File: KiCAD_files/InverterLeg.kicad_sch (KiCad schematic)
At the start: 61 parts, among them J803 Conn_01x01_Pin, J806 Conn_01x01_Pin, J811 Screw_Terminal_01x01, J814 Screw_Terminal_01x01, J817 Screw_Terminal_01x01, J825 Conn_02x02_Top_Bottom, J827 Conn_02x02_Top_Bottom, J831 Conn_02x02_Top_Bottom, Q801 IPT60R055CM8, Q802 IPT60R055CM8, T801 CMB1670V, T802 CMB1670V, U603 UCC21222DR, U704 VPS8701B, U707 VPS8701B, U811 TMP117xxDRV, U815 TMP117xxDRV

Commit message: First routing complete.
Signed-off-by: Jean Alinei <jean.alinei@owntech.org>
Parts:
- removed R710: 4.7k, Resistor_SMD:R_0603_1608Metric, symbol Device:R
- added C718, C719: 10uF, Capacitor_SMD:C_0805_2012Metric, symbol Device:C
- added R610, R611, R612, R613: 51R, Resistor_SMD:R_0402_1005Metric, symbol Device:R
- added U801, U802: LT1761-SD, Package_TO_SOT_SMD:TSOT-23-5, symbol Regulator_Linear:LT1761-SD
- U603: footprint Package_SO:SOIC-16W_7.5x10.3mm_P1.27mm -> Footprints:SOIC-16W_7.5x10.3mm_P1.27mm
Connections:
- net 12V_{HS}: now also C719.1, R610.2, U801.5 (VOUT); no longer C734.1, D709.1 (K), D710.1 (K)
- net 12V_{LS}: now also C718.1, R612.2, U802.5 (VOUT); no longer C717.1, C731.1, D703.1 (K), D704.1 (K), L706.1
- net GND_{LS}: now also C718.2, R613.1, U802.2 (GND)
- net K_{SWN}: now also C719.2, R611.1, U801.2 (GND)
- new net: C734.1, D709.1 (K), D710.1 (K), U801.1 (VIN), U801.3 (~{SHDN})
- new net: R610.1, R611.2, U801.4 (ADJ)
- new net: R612.1, R613.2, U802.4 (ADJ)
- new net 12V_{LSRAW}: C717.1, C731.1, D703.1 (K), D704.1 (K), L706.1, U802.1 (VIN), U802.3 (~{SHDN})

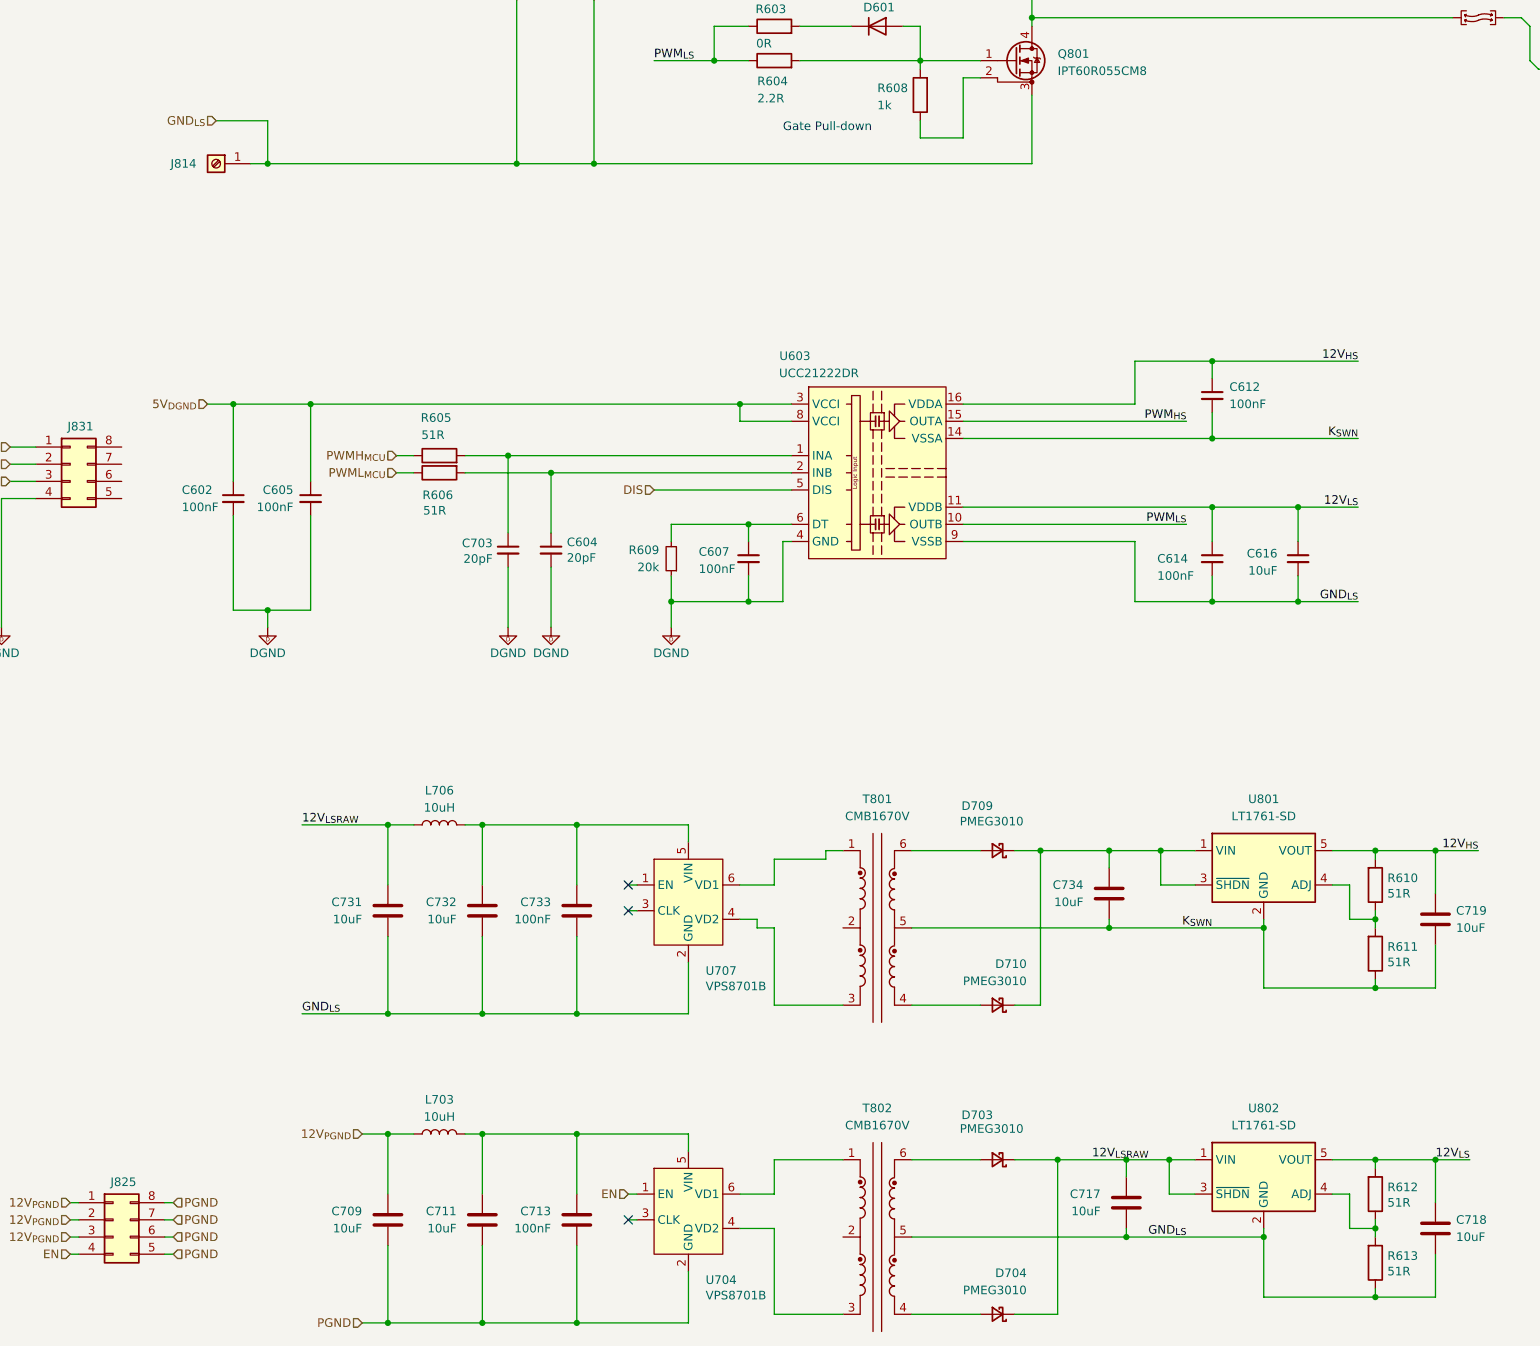
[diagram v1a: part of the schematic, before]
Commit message: Added gate coax. Added IPC2221 B1 rules. Changed diode footprints. Completed layout.
Signed-off-by: Jean Alinei <jean.alinei@owntech.org>
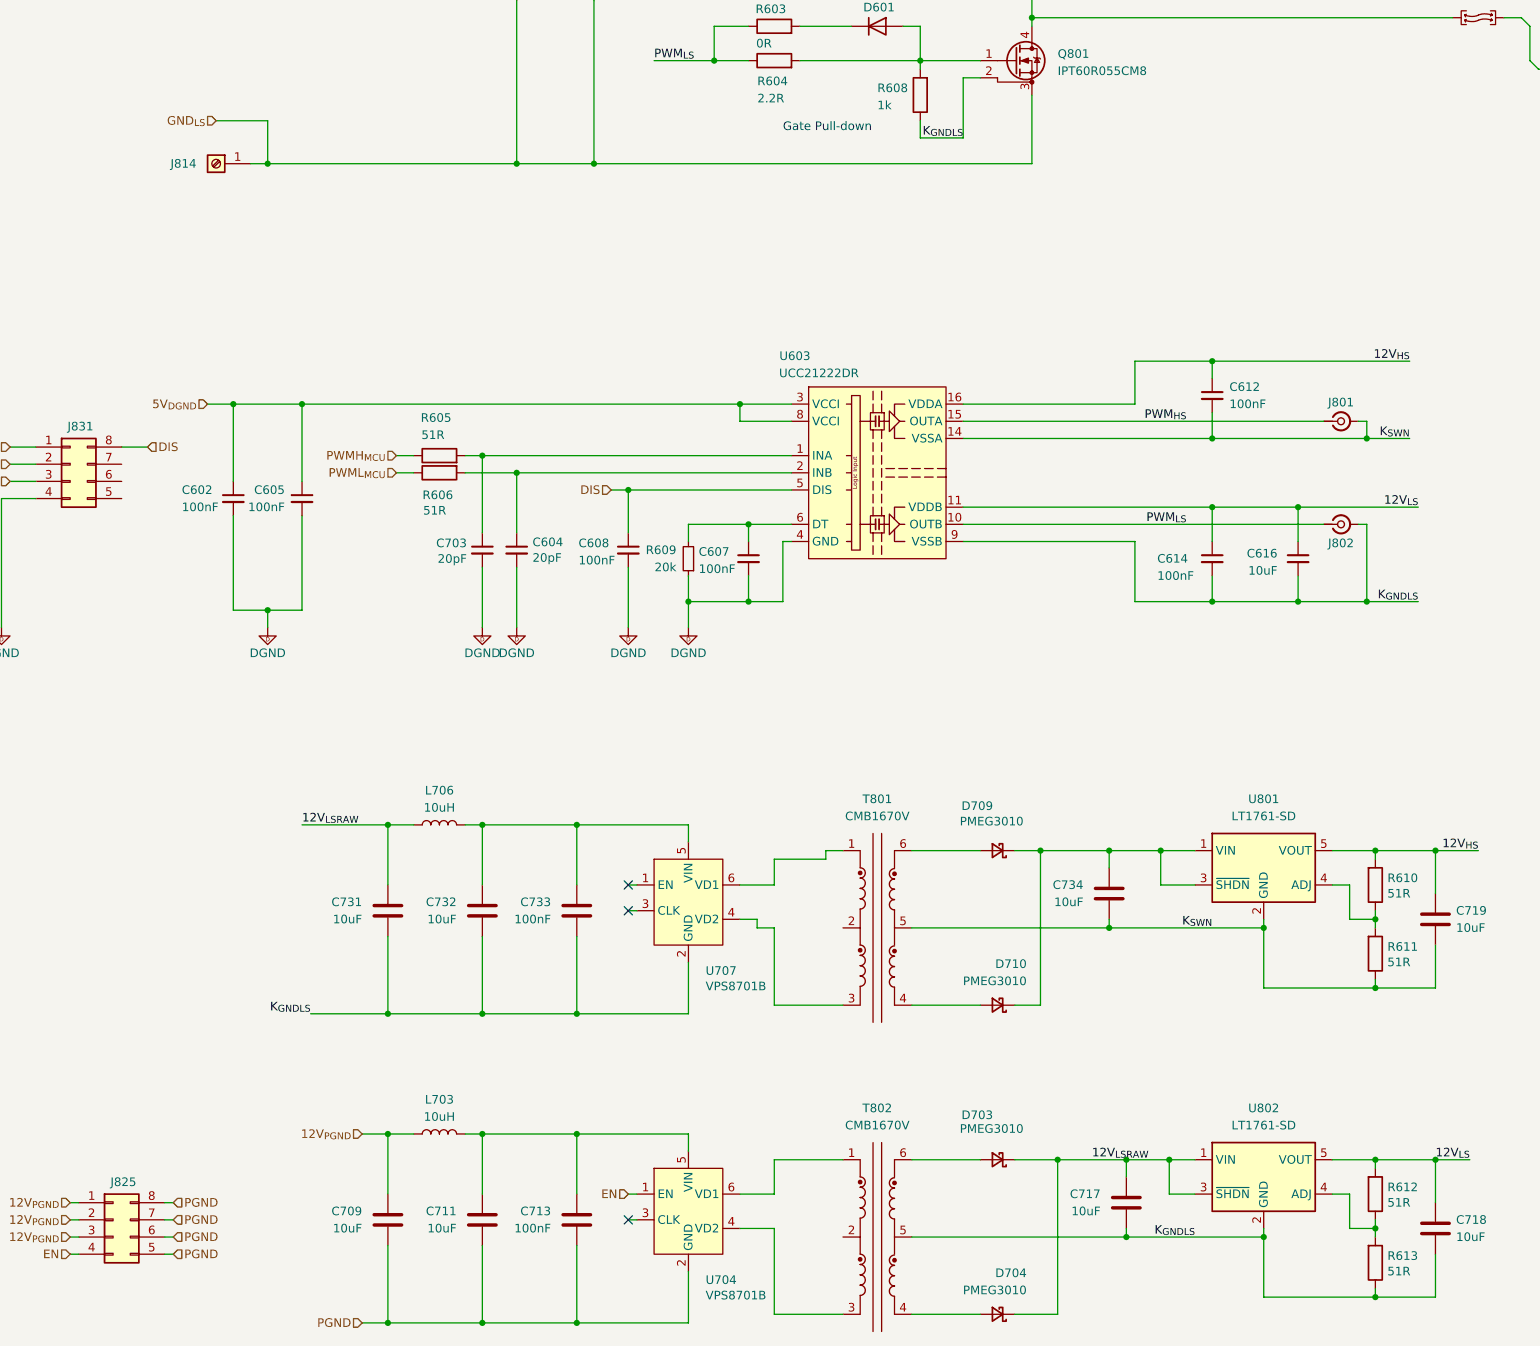
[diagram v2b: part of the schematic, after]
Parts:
- added C608: 100nF, Capacitor_SMD:C_0603_1608Metric, symbol Device:C_Small
- added J801, J802: Conn_Coaxial_Small, Footprints:IPEX-SMD_4P-L1.7-W1.7-LS2.0-L-4, symbol Symbols:Conn_Coaxial_Small
- D601: footprint Diode_SMD:D_SOD-323_HandSoldering -> Diode_SMD:D_SOD-882
- D602: value PMEG3010CEJ,115 -> (none); footprint Diode_SMD:D_SOD-323_HandSoldering -> Diode_SMD:D_SOD-882; manf# PMEG2010AEJ,115 -> (none)
- D703, D704, D709, D710: footprint Diode_SMD:D_SOD-323F -> Diode_SMD:D_SOD-882
- R607, R608: footprint Resistor_SMD:R_0603_1608Metric -> Resistor_SMD:R_0402_1005Metric
- TJ801, TJ804: footprint Resistor_SMD:R_1206_3216Metric -> Footprints:THJP_1206_3216Metric
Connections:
- net DGND: now also C608.2
- net DIS: now also J831.8 (Pin_8), C608.1
- net GND_{LS}: no longer C614.2, C616.2, C717.2, C718.2, C731.2, C732.2, C733.2, R613.1, T802.5, U603.9 (VSSB), U707.2 (GND), U802.2 (GND)
- net K_{SWN}: now also J801.2 (Ext), J801.3 (Ext), J801.4 (Ext)
- net PWM_{HS}: now also J801.1 (In)
- net PWM_{LS}: now also J802.1 (In)
- net K_{GNDLS}: now reaches Q801.2 (DS), R608.1
- net K_{GNDLS}: now also C614.2, C616.2, C717.2, C718.2, C731.2, C732.2, C733.2, R613.1, T802.5, U603.9 (VSSB), U707.2 (GND), U802.2 (GND), J802.2 (Ext), J802.3 (Ext), J802.4 (Ext)
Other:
- moved on the sheet: C604, C605, C703, R609

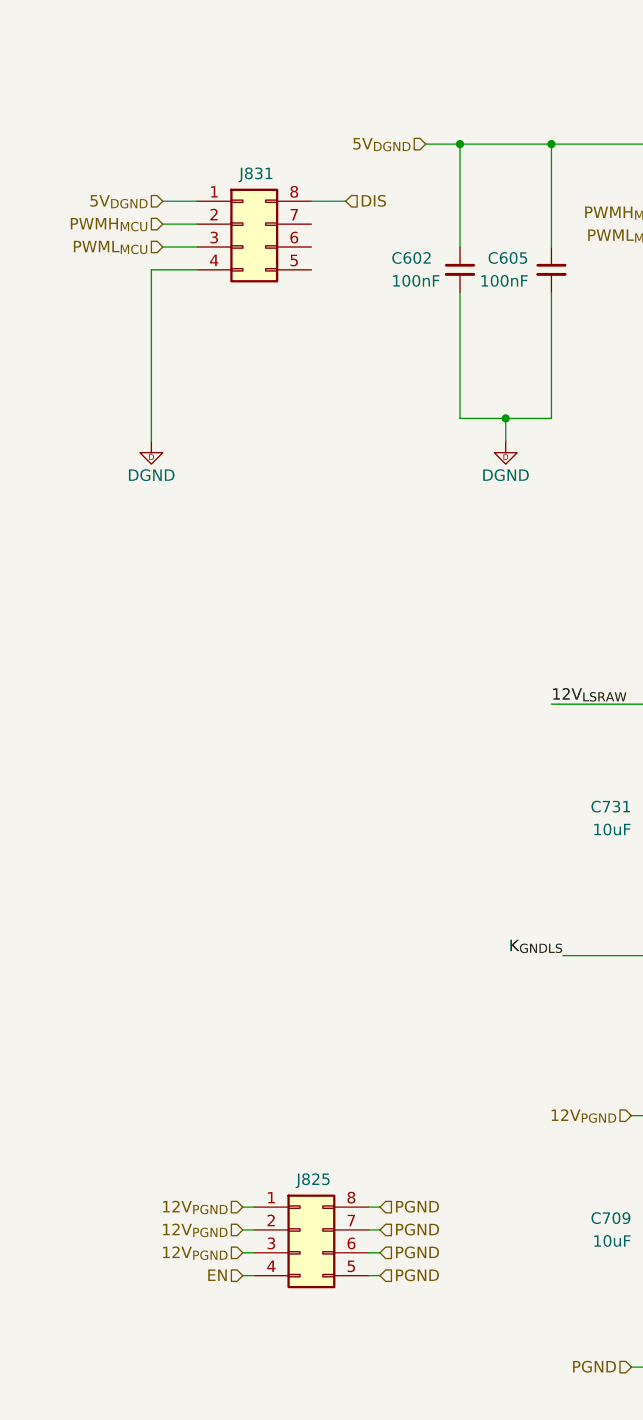
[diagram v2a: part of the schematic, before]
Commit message: Added SMTSO footprints to replace cube screw terminals. Added header for optional fan
Signed-off-by: Jean Alinei <jean.alinei@owntech.org>
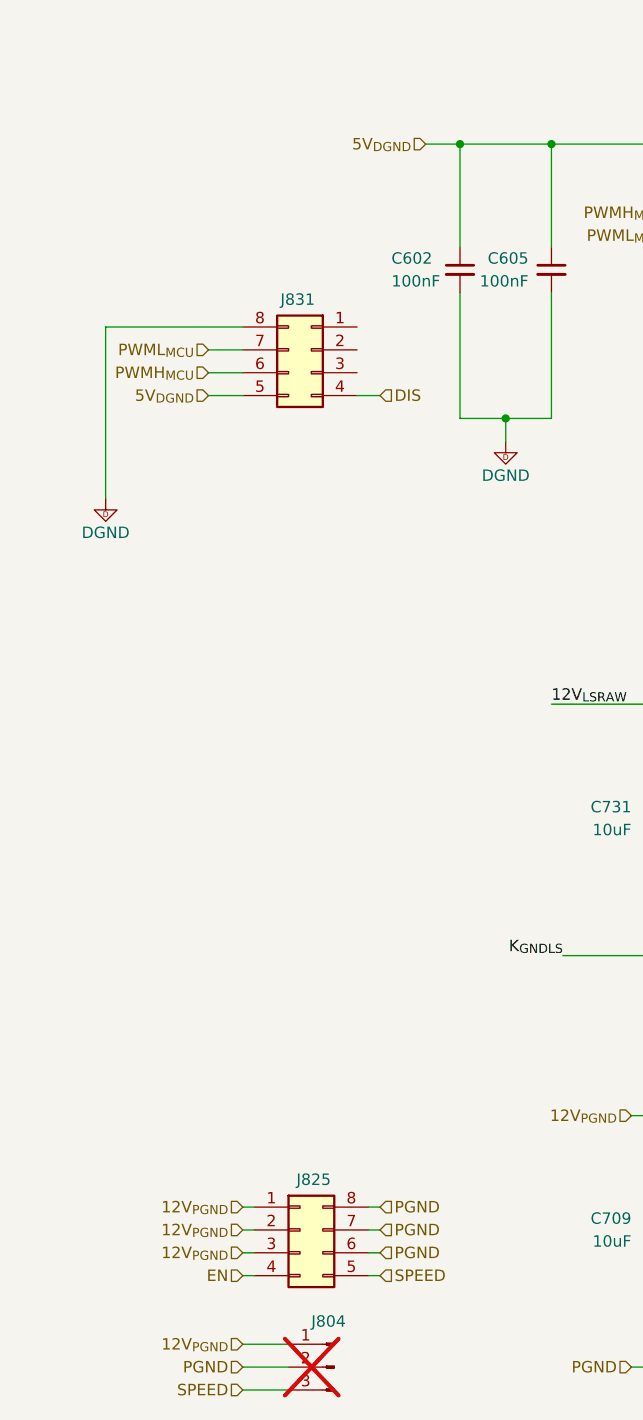
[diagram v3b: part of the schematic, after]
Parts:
- added J804: Conn_01x03_Socket, Connector_PinHeader_2.54mm:PinHeader_1x03_P2.54mm_Vertical, symbol Connector:Conn_01x03_Pin
- J801, J802: LCSC (none) -> C41432125
- J803, J806: LCSC (none) -> C54935091
- J811, J814, J817: footprint Footprints:SMD_L5.0-W5.0_CON1_5X5_SMD -> Footprints:SMD-1_BD5.5-D4.0_H5
- U801, U802: LCSC (none) -> C98119
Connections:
- net 12V_{PGND}: now also J804.1 (Pin_1)
- net 5V_{DGND}: now also J831.5 (Pin_5); no longer J831.1 (Pin_1)
- net DGND: now also J831.8 (Pin_8); no longer J831.4 (Pin_4)
- net DIS: now also J831.4 (Pin_4); no longer J831.8 (Pin_8)
- net PGND: now also J804.2 (Pin_2); no longer J825.5 (Pin_5)
- net PWMH_{MCU}: now also J831.6 (Pin_6); no longer J831.2 (Pin_2)
- net PWML_{MCU}: now also J831.7 (Pin_7); no longer J831.3 (Pin_3)
- new net SPEED: J804.3 (Pin_3), J825.5 (Pin_5)

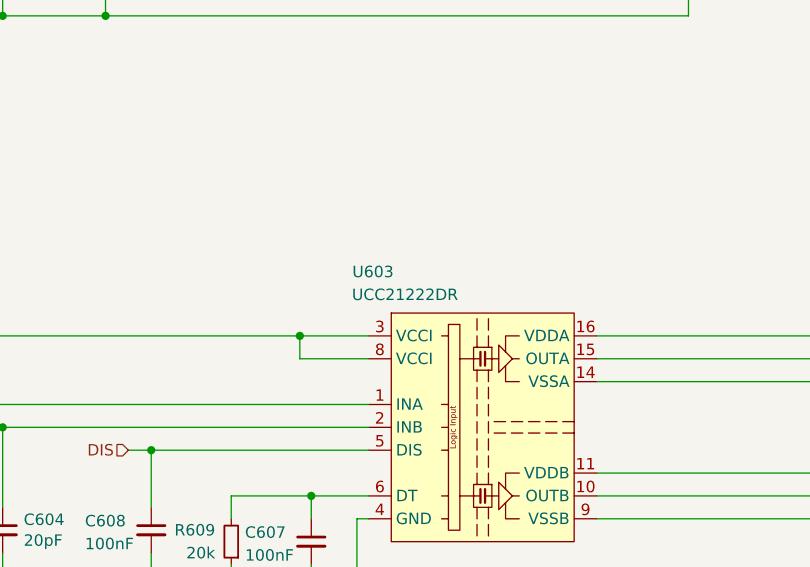
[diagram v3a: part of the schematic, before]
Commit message: Tidied up schematic - Final height for SMTSO 5mm
Signed-off-by: Jean Alinei <jean.alinei@owntech.org>
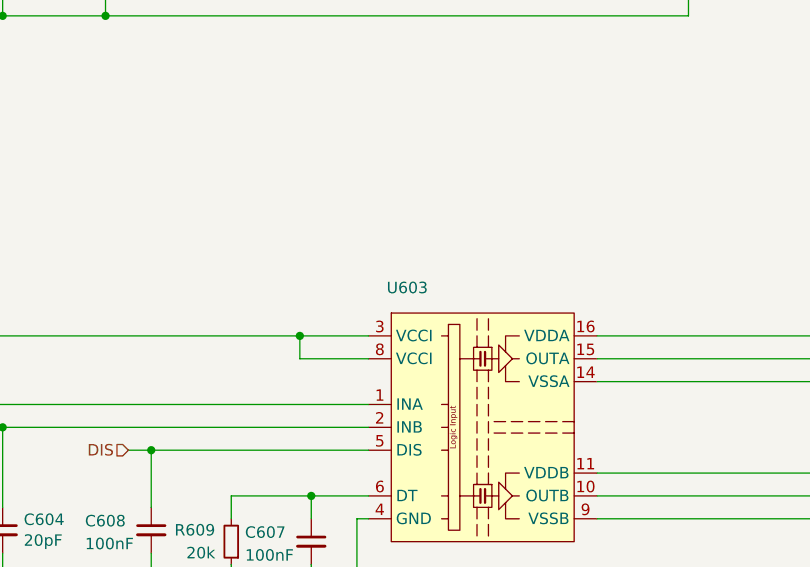
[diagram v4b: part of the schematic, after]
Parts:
- U603: value UCC21222DR -> (none); Reserved1 bccaf22d96de636e419712282ae246d314e74c1c3b4854d5 -> (none); manf# UCC21222DR -> (none)
- U704: LCSC (none) -> C5189123; Reserved1 54ac28721298fbc865f2e5f34cb150e57d7a5c0d0331fcf6 -> (none)
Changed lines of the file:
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@@
 		(dnp no)
 		(property "Reference" "U603"
-			(at 175.768 119.888 0)
-			(show_name no)
-			(do_not_autoplace no)
-			(effects
-				(font
-					(size 1.27 1.27)
-				)
-			)
-		)
-		(property "Value" "UCC21222DR"
+			(at 179.578 121.666 0)
+			(show_name no)
+			(do_not_autoplace no)
+			(effects
+				(font
+					(size 1.27 1.27)
+				)
+			)
+		)
+		(property "Value" ""
 			(at 179.324 122.428 0)
 			(show_name no)
@@
 		)
 		(property "Description" ""
-			(at 187.96 134.62 0)
-			(hide yes)
-			(show_name no)
-			(do_not_autoplace no)
-			(effects
-				(font
-					(size 1.27 1.27)
-				)
-			)
-		)
-		(property "manf#" "UCC21222DR"
-			(at 187.96 134.62 0)
-			(hide yes)
-			(show_name no)
-			(do_not_autoplace no)
-			(effects
-				(font
-					(size 1.27 1.27)
-				)
-			)
-		)
-		(property "Reserved1" "bccaf22d96de636e419712282ae246d314e74c1c3b4854d5"
 			(at 187.96 134.62 0)
 			(hide yes)
@@
 			)
 		)
-		(property "Reserved1" "54ac28721298fbc865f2e5f34cb150e57d7a5c0d0331fcf6"
-			(at 160.02 246.38 0)
-			(hide yes)
-			(show_name no)
-			(do_not_autoplace no)
-			(effects
-				(font
-					(size 1.27 1.27)
-				)
-			)
-		)
 		(property "Rotation Offset" "90"
 			(at 160.02 246.38 0)
 			(hide yes)
+			(show_name no)
+			(do_not_autoplace no)
+			(effects
+				(font
+					(size 1.27 1.27)
+				)
+			)
+		)
+		(property "LCSC" "C5189123"
+			(at 160.02 246.38 0)
+			(hide yes)

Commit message: the schematic has no more ERC and the DRC are on their way
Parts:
- D601, D602: LCSC (none) -> C28646370; Reserved1 43817ac0f4fec423c7625c960c4fb4ef1e3331450741e4 -> (none)
- D703, D704, D709, D710: LCSC (none) -> C28646370; Reserved1 b290c14b85873ea809465af0ca5e7363b6ac9827ec701874 -> (none)
- J811, J814, J817: LCSC (none) -> C2915636
- J825, J827, J831: value Conn_02x02_Top_Bottom -> HC-PBB08-2-08-M-H4.0-G1-R-P-04; LCSC (none) -> C41421136
- L703, L706: LCSC (none) -> C88173; Reserved1 96cc0daa239b4529f4515b08987c268f246fc82db8ff -> (none)
- Q801, Q802: LCSC (none) -> C47146866
- R609: LCSC (none) -> C4328; Reserved1 4e62068438486240cd804b758ba9b5cf82f9e4c51a -> (none)
- R610: value 51R -> 176.8k
- R611, R613: value 51R -> 20k; Reserved1 09f3912dc83c8a80315b578c251a24aaa57a6fa6cfa9 -> (none)
- R612: value 51R -> 176.8k; Reserved1 09f3912dc83c8a80315b578c251a24aaa57a6fa6cfa9 -> (none)
- TJ801, TJ804: LCSC (none) -> C3029094
- U707: LCSC (none) -> C5189123; Reserved1 54ac28721298fbc865f2e5f34cb150e57d7a5c0d0331fcf6 -> (none)
- U811, U815: LCSC (none) -> C5447196
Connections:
- net 5V_{PGND} is gone; now on net +5V_PGND: C751.1, C754.1, U811.5 (V+), U815.5 (V+)
- net EN: now also J825.8 (Pin_8); no longer J825.4 (Pin_4)
- net PGND: no longer C709.2, C711.2, C713.2, J804.2 (Pin_2), J825.6 (Pin_6), J825.7 (Pin_7), J825.8 (Pin_8), U704.2 (GND)
- net SPEED: now also J825.4 (Pin_4); no longer J825.5 (Pin_5)
- net 12V_{PGND} renamed +12V_PGND
- net 5V_{DGND} renamed +5V_DGND
- net 5V_{LS} renamed +5V_PGND
- removed net Earth_Protective: H801.1, H802.1, H803.1, H804.1, J803.1 (Pin_1), J806.1 (Pin_1)
- new net Earth_Protective1: H801.1
- new net Earth_Protective2: H802.1, J806.1 (Pin_1)
- new net Earth_Protective3: H803.1, J803.1 (Pin_1)
- new net Earth_Protective4: H804.1
- new net PGND2: C709.2, C711.2, C713.2, J804.2 (Pin_2), J825.5 (Pin_5), J825.6 (Pin_6), J825.7 (Pin_7), U704.2 (GND)
- no-connect marks 3 -> 8
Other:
- note added: "DT (in ns) = 10 × R_{DT} (in kΩ). TI recommends bypassing this pin with a ceramic capacitor, 2.2 nF or greater. So with DT = @{10*(${/8d0c1d66-35ef-4a53-a28f-436a11b54f42/532bac1e-414d-4f10-8c4a-d2334bc02fa5:Value}/1000)}nS"
- note added: "FAN HEADER"
- note added: "INA & INB have 200kΩ internal pulldown and DIS has a 50kΩ internal pulldown"
- note added: "J801 and J802 for easy gate probing"
- note added: "TI recommends adding a small ceramic capacitor between DIS and gnd to improve noise immunity, 1 nF or greater."
- note added: "The VPS8701B is enabled when EN is floating or pulled up. It is DISABLED when connected to GND"
- note added: "V_{OUT} = VADJ (1 + (R612/R613)) + (I_{ADJ} * R612) V_{ADJ} = 1.22V I_{ADJ} = 30nA at 25°C So: V_{OUT} = @{round((1.22*(1+(${/8d0c1d66-35ef-4a53-a28f-436a11b54f42/153ae966-be28-4ef2-b43e-ea2e9beaff1f:Value}/${/8d0c1d66-35ef-4a53-a28f-436a11b54f42/9b8227a6-f6d8-4461-b56f-2b44b0c1a3de:Value}))+(0.00000003*${/8d0c1d66-35ef-4a53-a28f-436a11b54f42/153ae966-be28-4ef2-b43e-ea2e9beaff1f:Value}))*100)/100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"
- note added: "WHY only this transformer has an ENABLE signal??"
- note added: "When the DIS pin is set high, both outputs are shut down simultaneously"
- moved on the sheet: C602, C604, C605, C608, C703, C709, C711, C713, C717, C718, C751, C754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
